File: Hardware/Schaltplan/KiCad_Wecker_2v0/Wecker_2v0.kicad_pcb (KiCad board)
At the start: 2 copper layers, 28 parts

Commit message: Firmware 20v29: Ausgangs-GPIOs E1/E2/E3 getauscht (Schaltplan-Update Hardware 2v0)
Kuckuck (E1) GPIO25->GPIO27, DC-Motor/Muehlrad (E2) GPIO26->GPIO25,
LED-Streifen/Licht (E3) GPIO27->GPIO26. In der Firmware nur die Zahlenwerte
der E1/E2/E3-Konstanten in SysConf_20v29.h geaendert - die Ansteuerlogik
(digitalWrite, ledcAttach/ledcWrite, motorStart/motorStop, runCuckooMachine,
S2-Zugschalter, /motor-Handler) nutzt ausschliesslich die symbolischen
Konstanten und ist unveraendert. Motor-PWM-Kanal wandert von GPIO26 auf GPIO25.

Dokumentation nachgezogen: CHANGELOG, CLAUDE.md, README.md, Schaltplan-Notizen
(Motor-Treiber, Motor-LED-Treiber_Bauteilnotizen, Schaltplan/README).
KiCad-Schaltplan Hardware 2v0 mit aktualisierter Pin-Belegung.

Co-Authored-By: Claude Sonnet 5 <noreply@anthropic.com>
Claude-Session: https://claude.ai/code/session_01YD1NFKu8eXrE6EPc1gn86D
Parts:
- removed MCP1700T-1502E/MB: SOT-89-3, Package_TO_SOT_SMD:SOT-89-3
- added DFPLAYER1: DFPLAYER, DFPlayer:DFPlayerMini, F.Cu at (69.8, 138.4)
- added REF**: ws USB-, Connector_Pin:Pin_D1.0mm_L10.0mm, F.Cu at (74.9, 156.2)
- added REF**: R_Axial_DIN0207_L6.3mm_D2.5mm_P10.16mm_Horizontal, Resistor_THT:R_Axial_DIN0207_L6.3mm_D2.5mm_P10.16mm_Horizontal, F.Cu at (31.8, 62.2)
- added REF**: CP_Radial_D10.0mm_P5.00mm, Capacitor_THT:CP_Radial_D10.0mm_P5.00mm, F.Cu at (54.5, 146.1)
- added REF**: ws USB-, Connector_Pin:Pin_D1.0mm_L10.0mm, F.Cu at (74.9, 151.1)
- added REF**: RX, Connector_Pin:Pin_D1.0mm_L10.0mm, F.Cu at (36.8, 74.9)
- added REF**: RX, Connector_Pin:Pin_D1.0mm_L10.0mm, F.Cu at (59.7, 133.3)
- added REF**: TSOT-23, Package_TO_SOT_SMD:TSOT-23, F.Cu at (40.6, 129.5)
- added REF**: TO-92L_Inline_Wide, Package_TO_SOT_THT:TO-92L_Inline_Wide, F.Cu at (52.1, 130.8)
- added REF**: 10µF, Capacitor_THT:C_Disc_D3.0mm_W1.6mm_P2.50mm, F.Cu at (67.3, 148.6)
- added REF**: RX, Connector_Pin:Pin_D1.0mm_L10.0mm, F.Cu at (29.2, 120.7)
- added REF**: RX, Connector_Pin:Pin_D1.0mm_L10.0mm, F.Cu at (39.4, 128.3)
- added REF**: R_Axial_DIN0207_L6.3mm_D2.5mm_P10.16mm_Horizontal, Resistor_THT:R_Axial_DIN0207_L6.3mm_D2.5mm_P10.16mm_Horizontal, F.Cu at (34.3, 54.6)
- added REF**: R_Axial_DIN0207_L6.3mm_D2.5mm_P10.16mm_Horizontal, Resistor_THT:R_Axial_DIN0207_L6.3mm_D2.5mm_P10.16mm_Horizontal, F.Cu at (36.8, 153.7)
- added REF**: R_Axial_DIN0207_L6.3mm_D2.5mm_P10.16mm_Horizontal, Resistor_THT:R_Axial_DIN0207_L6.3mm_D2.5mm_P10.16mm_Horizontal, F.Cu at (31.8, 113.0)
- added REF**: 47µ/16V, Capacitor_THT:CP_Radial_D5.0mm_P2.50mm, F.Cu at (62.3, 148.7)
- added REF**: RX, Connector_Pin:Pin_D1.0mm_L10.0mm, F.Cu at (85.1, 130.8)
- added REF**: RX, Connector_Pin:Pin_D1.0mm_L10.0mm, F.Cu at (85.1, 62.2)
- added REF**: TX, Connector_Pin:Pin_D1.0mm_L10.0mm, F.Cu at (67.3, 133.3)
- added REF**: 22nF, Capacitor_THT:C_Disc_D3.0mm_W1.6mm_P2.50mm, F.Cu at (80.0, 130.8)
- added REF**: TSOT-23, Package_TO_SOT_SMD:TSOT-23, F.Cu at (30.5, 38.1)
- added REF**: RX, Connector_Pin:Pin_D1.0mm_L10.0mm, F.Cu at (85.1, 138.4)
- added REF**: R_Axial_DIN0207_L6.3mm_D2.5mm_P10.16mm_Horizontal, Resistor_THT:R_Axial_DIN0207_L6.3mm_D2.5mm_P10.16mm_Horizontal, F.Cu at (34.3, 133.3)
- added REF**: TSOT-23, Package_TO_SOT_SMD:TSOT-23, F.Cu at (40.6, 38.1)
- added REF**: TSOT-23, Package_TO_SOT_SMD:TSOT-23, F.Cu at (40.6, 144.8)
- added REF**: R_Axial_DIN0207_L6.3mm_D2.5mm_P10.16mm_Horizontal, Resistor_THT:R_Axial_DIN0207_L6.3mm_D2.5mm_P10.16mm_Horizontal, F.Cu at (31.8, 118.1)
- added REF**: RX, Connector_Pin:Pin_D1.0mm_L10.0mm, F.Cu at (77.5, 130.8)
- added REF**: Motor, Connector_Pin:Pin_D1.0mm_L10.0mm, F.Cu at (39.4, 143.5)
- added REF**: R_Axial_DIN0207_L6.3mm_D2.5mm_P10.16mm_Horizontal, Resistor_THT:R_Axial_DIN0207_L6.3mm_D2.5mm_P10.16mm_Horizontal, F.Cu at (31.8, 133.3)
- added REF**: R_Axial_DIN0207_L6.3mm_D2.5mm_P10.16mm_Horizontal, Resistor_THT:R_Axial_DIN0207_L6.3mm_D2.5mm_P10.16mm_Horizontal, F.Cu at (31.8, 115.6)
- added REF**: CP_Radial_D8.0mm_P2.50mm, Capacitor_THT:CP_Radial_D8.0mm_P2.50mm, F.Cu at (54.6, 138.4)
- added REF**: R_Axial_DIN0207_L6.3mm_D2.5mm_P10.16mm_Horizontal, Resistor_THT:R_Axial_DIN0207_L6.3mm_D2.5mm_P10.16mm_Horizontal, F.Cu at (31.8, 54.6)
- added REF**: RX, Connector_Pin:Pin_D1.0mm_L10.0mm, F.Cu at (34.3, 120.7)
- added REF**: R_Axial_DIN0207_L6.3mm_D2.5mm_P10.16mm_Horizontal, Resistor_THT:R_Axial_DIN0207_L6.3mm_D2.5mm_P10.16mm_Horizontal, F.Cu at (36.8, 54.6)
- added REF**: TSOT-23, Package_TO_SOT_SMD:TSOT-23, F.Cu at (40.6, 137.2)
- added REF**: R_Axial_DIN0207_L6.3mm_D2.5mm_P10.16mm_Horizontal, Resistor_THT:R_Axial_DIN0207_L6.3mm_D2.5mm_P10.16mm_Horizontal, F.Cu at (62.2, 133.3)
- added REF**: TO-92L_Inline_Wide, Package_TO_SOT_THT:TO-92L_Inline_Wide, F.Cu at (41.9, 69.8)
- added REF**: TSOT-23, Package_TO_SOT_SMD:TSOT-23, F.Cu at (35.6, 38.1)
- added REF**: R_Axial_DIN0207_L6.3mm_D2.5mm_P10.16mm_Horizontal, Resistor_THT:R_Axial_DIN0207_L6.3mm_D2.5mm_P10.16mm_Horizontal, F.Cu at (64.8, 133.3)
- added REF**: R_Axial_DIN0207_L6.3mm_D2.5mm_P10.16mm_Horizontal, Resistor_THT:R_Axial_DIN0207_L6.3mm_D2.5mm_P10.16mm_Horizontal, F.Cu at (31.8, 59.7)
- added REF**: R_Axial_DIN0207_L6.3mm_D2.5mm_P10.16mm_Horizontal, Resistor_THT:R_Axial_DIN0207_L6.3mm_D2.5mm_P10.16mm_Horizontal, F.Cu at (31.8, 57.1)
- added REF**: R_Axial_DIN0207_L6.3mm_D2.5mm_P10.16mm_Horizontal, Resistor_THT:R_Axial_DIN0207_L6.3mm_D2.5mm_P10.16mm_Horizontal, F.Cu at (29.2, 133.3)
- added REF**: RX, Connector_Pin:Pin_D1.0mm_L10.0mm, F.Cu at (39.4, 135.9)
- added REF**: R_Axial_DIN0207_L6.3mm_D2.5mm_P10.16mm_Horizontal, Resistor_THT:R_Axial_DIN0207_L6.3mm_D2.5mm_P10.16mm_Horizontal, F.Cu at (29.2, 54.6)
- added REF**: RX, Connector_Pin:Pin_D1.0mm_L10.0mm, F.Cu at (31.8, 120.7)
- REF**: value ws USB- -> TX
- REF**: value 22nF -> 10µF
- REF**: value ws USB- -> RX
- moved REF** 7.62 mm to (41.9, 74.9)
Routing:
- net (no net): track 237.3 -> 688.8 mm
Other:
- board text added: "1,5V Analoguhr"
- board text added: "ACHTUNG MOSFET über Kopf auf Lötseite"
- board text added: "BUSY"
- board text added: "C13 10µF"
- board text added: "C3 1000µF"
- board text added: "C4 2200µF"
- board text added: "C5 22nF"
- board text added: "C6 10µF"
- board text added: "GPIO 25 26 27"
- board text added: "Motor"
- board text added: "Player-Modul"
- board text added: "R1 100 R2 100 R3 100"
- board text added: "R14 33k"
- board text added: "R4 10k R5 10k R6 10k"
- board text added: "R8 100"
- board text added: "R9 100"
- board text added: "U2 DFPlayer mini"
- board text added: "U4 MCP1702-1502TO"
- board text added: "Vout 1,5V"

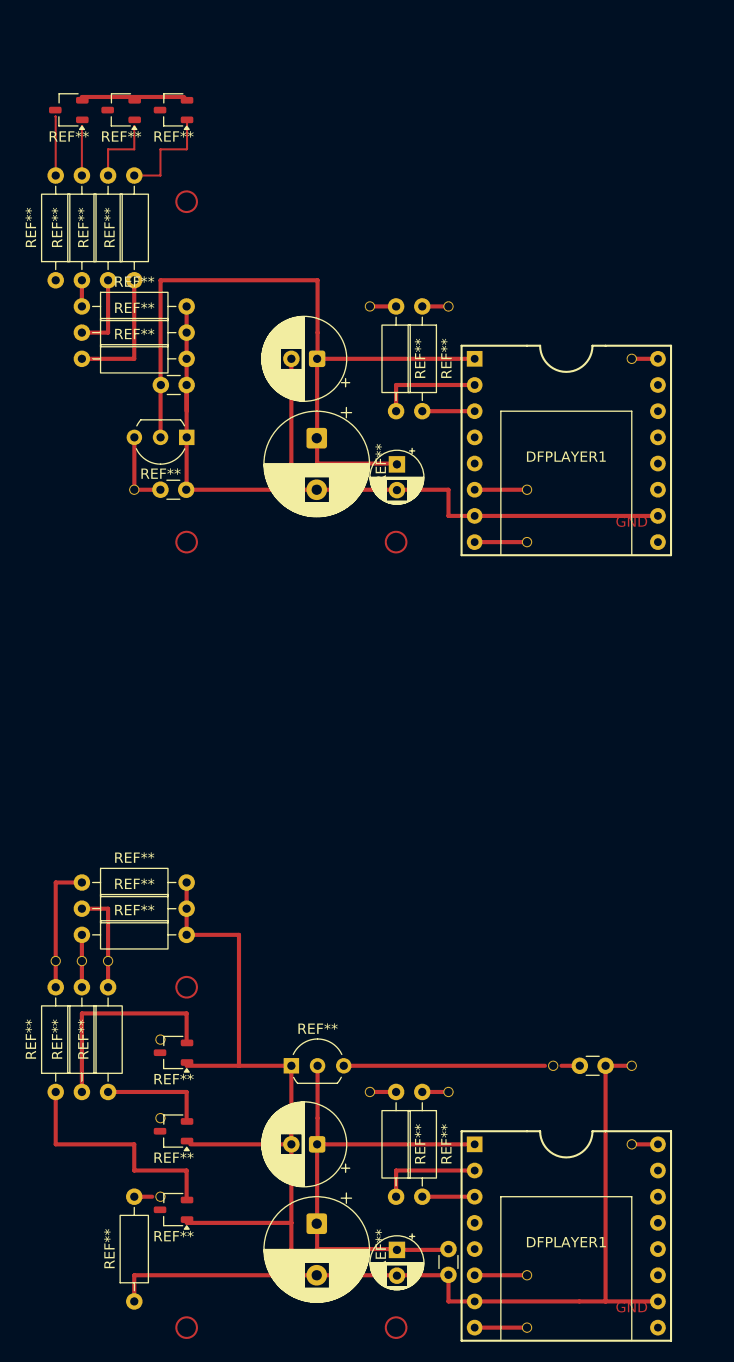
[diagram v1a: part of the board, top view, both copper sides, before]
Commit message: KiCad 2v0: Gate-Widerstände R1/R2/R3 auf 470Ω, E1/E2/E3-Label aktualisiert
Gate-Reihenwiderstände der drei IRLML6344-MOSFETs (Q1/Q2/Q3) standen im
Schaltplan-Symbol noch auf 100Ω statt der dokumentierten 330Ω – jetzt
konsistent mit Stückliste/Schaltplan-Notizen auf 470Ω gesetzt.
Dazu Textlabel für E1/E2/E3-Funktionsbeschriftung aktualisiert sowie
Positionsfeinjustierung C9/C11.

Co-Authored-By: Claude Sonnet 5 <noreply@anthropic.com>
Claude-Session: https://claude.ai/code/session_01PFX3jg5htPhYmZCUmWU2SY
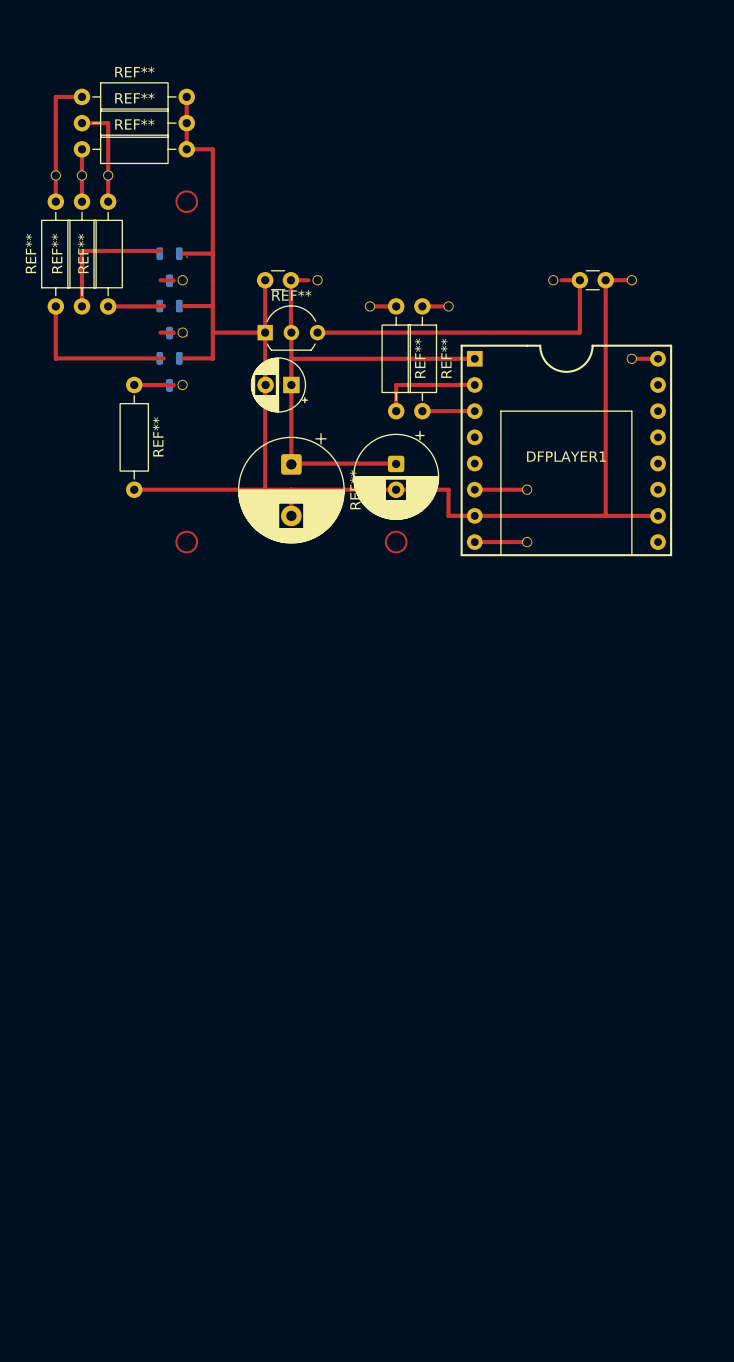
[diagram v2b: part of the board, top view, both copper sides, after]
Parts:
- removed the DFPLAYER1 at (69.8, 62.2)
- removed the REF** at (31.8, 62.2)
- removed the REF** at (36.8, 74.9)
- removed the REF** at (41.9, 74.9)
- removed the REF** at (34.3, 54.6)
- removed the REF** at (64.8, 57.1)
- removed the REF** at (67.3, 57.1)
- removed the REF** at (85.1, 62.2)
- removed the REF** at (62.3, 72.5)
- removed the REF** at (30.5, 38.1)
- removed the REF** at (74.9, 74.9)
- removed the REF** at (41.9, 64.8)
- removed the REF** at (40.6, 38.1)
- removed the REF** at (31.8, 54.6)
- removed the REF** at (36.8, 54.6)
- removed the REF** at (54.6, 62.2)
- removed the REF** at (62.2, 57.1)
- removed the REF** at (41.9, 69.8)
- removed the REF** at (59.7, 57.1)
- removed the REF** at (74.9, 80.0)
- removed the REF** at (35.6, 38.1)
- removed the REF** at (31.8, 59.7)
- removed the REF** at (54.5, 69.9)
- removed the REF** at (31.8, 57.1)
- removed the REF** at (29.2, 54.6)
- added REF**: RX, Connector_Pin:Pin_D1.0mm_L10.0mm, F.Cu at (54.6, 54.6)
- REF** (x6): moved to B.Cu
- moved REF** 95.6 mm to (49.5, 54.6), turned to 0 degrees
- moved REF** 88.9 mm to (36.8, 64.8), turned to -90 degrees
- moved REF** 84.5 mm to (52.1, 64.8), turned to 180 degrees
- moved REF** 81.3 mm to (40.2, 63.5), turned to -90 degrees
- moved REF** 78.8 mm to (41.5, 64.8)
- moved REF** 78.7 mm to (40.2, 58.4), turned to -90 degrees
- moved REF** 76.2 mm to (41.5, 59.7)
- moved REF** 76.2 mm to (40.2, 53.3), turned to -90 degrees
- moved REF** 76.2 mm to (74.9, 80.0)
- moved DFPLAYER1 76.2 mm to (69.9, 62.2)
- moved REF** 76.2 mm to (29.2, 44.4)
- moved REF** 76.2 mm to (31.8, 36.8)
- moved REF** 76.2 mm to (67.3, 57.1)
- moved REF** 76.2 mm to (80.1, 54.6)
- moved REF** 76.2 mm to (85.1, 62.2)
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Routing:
- net (no net): track 688.8 -> 427.2 mm
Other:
- board text added: "5V"
- board text added: "Cuckoo"
- board text added: "LED"
- board text added: "Vin"
- board text added: "Vout"
- board text removed: "Vout 1,5V"

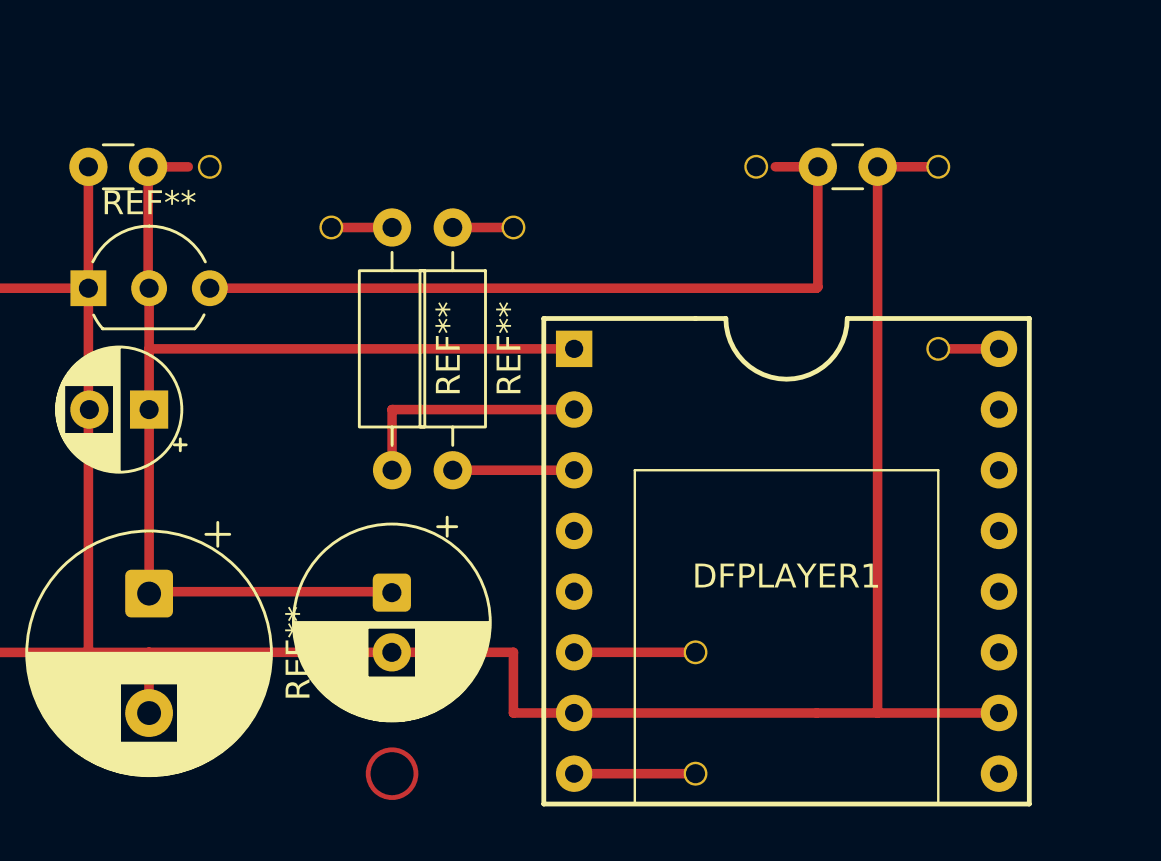
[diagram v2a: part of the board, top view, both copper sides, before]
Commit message: KiCad 2v0: DFPlayer-BUSY-Filter (R15/C14) und weitere Layout-Änderungen
Übernimmt den aktuellen KiCad-Bearbeitungsstand: neue Bauteile R15
(1kΩ), C6, C14 (100nF/4,7µF) sowie zugehörige PCB-Layout-Änderungen.

Co-Authored-By: Claude Sonnet 5 <noreply@anthropic.com>
Claude-Session: https://claude.ai/code/session_01PFX3jg5htPhYmZCUmWU2SY
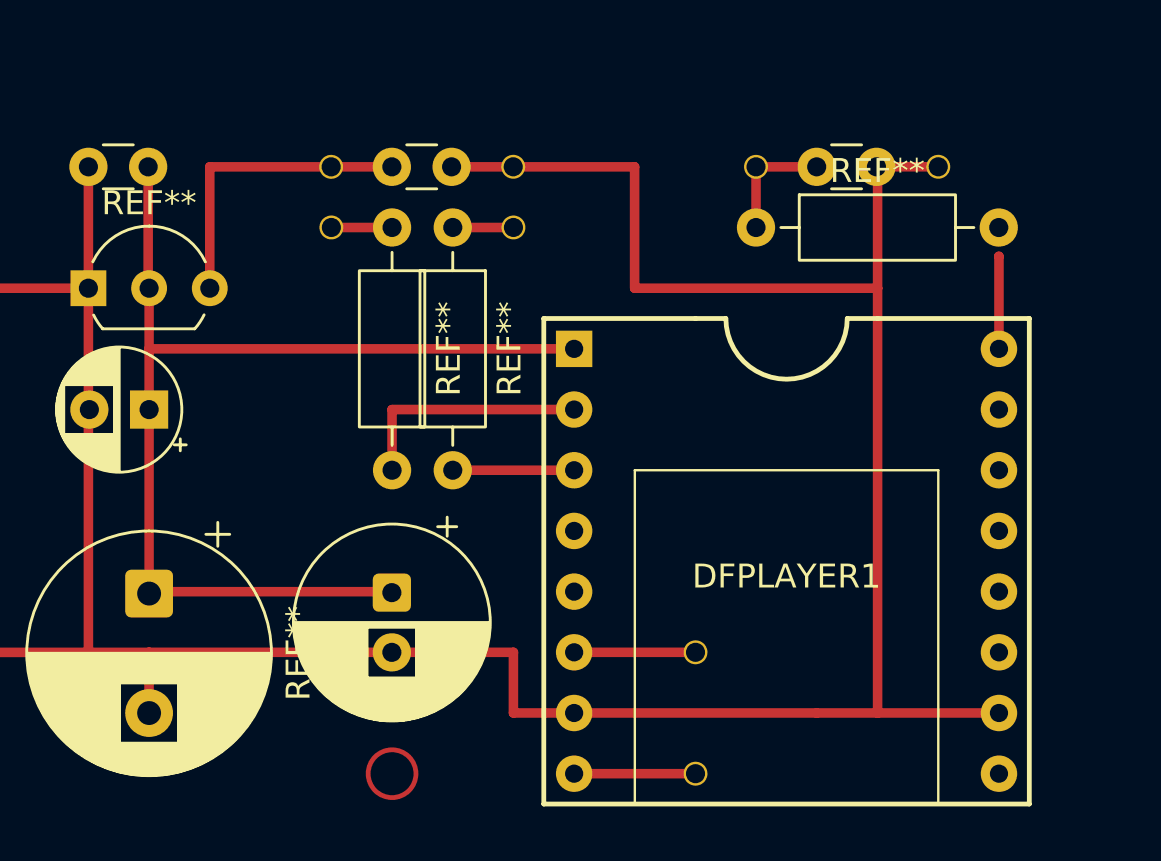
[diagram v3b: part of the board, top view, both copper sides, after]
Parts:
- added REF**: R_Axial_DIN0207_L6.3mm_D2.5mm_P10.16mm_Horizontal, Resistor_THT:R_Axial_DIN0207_L6.3mm_D2.5mm_P10.16mm_Horizontal, F.Cu at (77.5, 57.1)
- added REF**: 22nF, Capacitor_THT:C_Disc_D3.0mm_W1.6mm_P2.50mm, F.Cu at (80.0, 54.6)
- moved REF** 17.8 mm to (62.2, 54.6)
- moved REF** 10.8 mm to (77.5, 54.6)
- moved REF** 10.2 mm to (67.3, 54.6)
- moved REF** 5.08 mm to (59.7, 54.6)
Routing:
- net (no net): track 427.2 -> 437.1 mm
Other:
- board text added: "C14 100nF"
- board text added: "C6 4,7µF"
- board text added: "R1 470 R2 470 R3 470"
- board text added: "R15 1k"
- board text removed: "C6 10µF"
- board text removed: "R1 100 R2 100 R3 100"
